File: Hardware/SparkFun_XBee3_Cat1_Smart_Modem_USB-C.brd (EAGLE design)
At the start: 35.6 x 59.7 mm, 107 parts, among them J3 USB Female Type C Connector, J4 QWIIC_RIGHT_ANGLE, U2 AP63203, U5 ESD Diode, U7 FT231XS

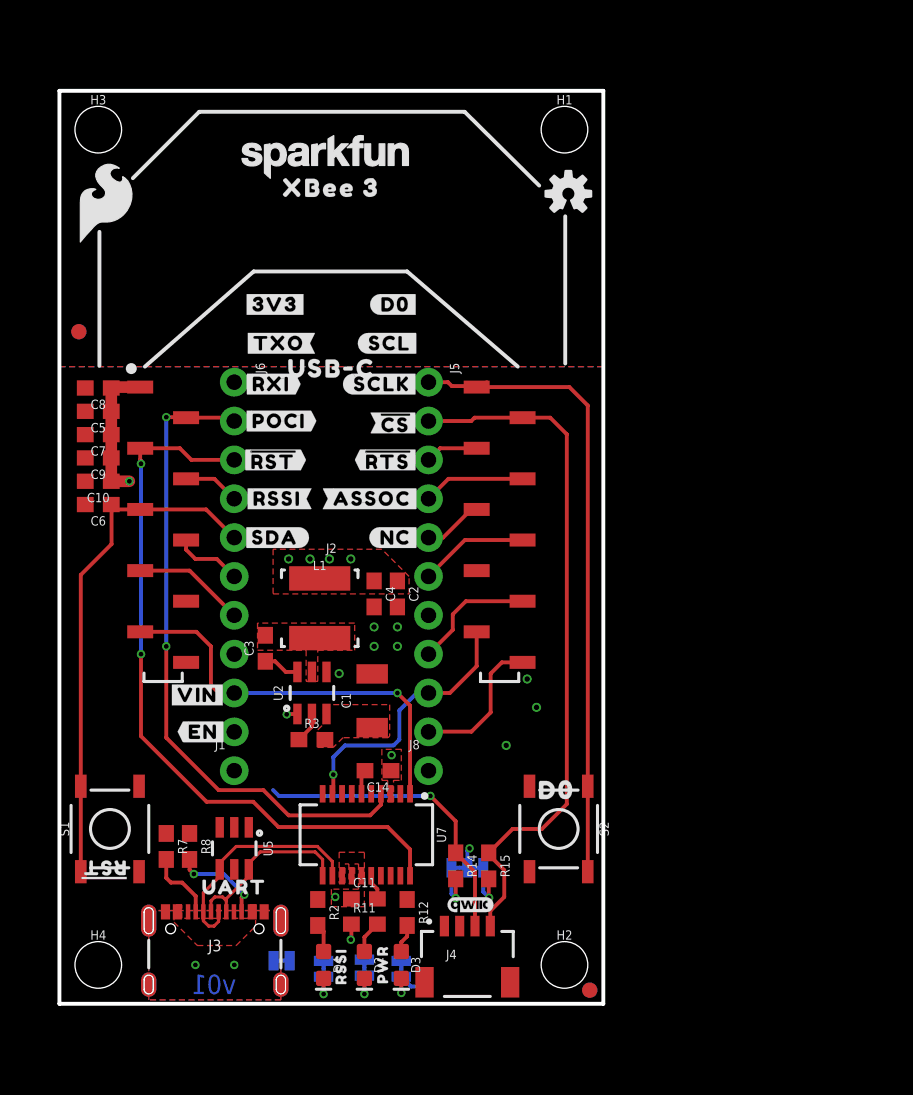
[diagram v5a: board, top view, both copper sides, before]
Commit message: Finishes routing airwires, fixes silk
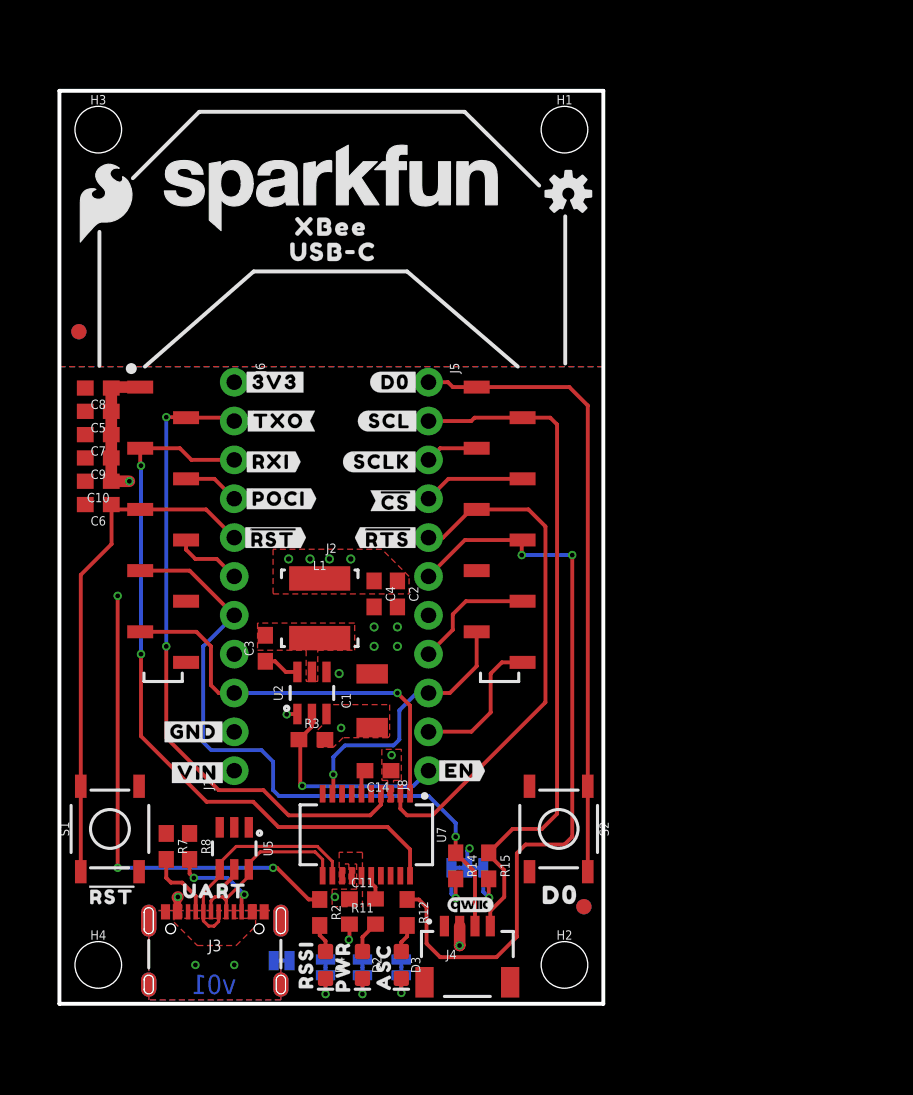
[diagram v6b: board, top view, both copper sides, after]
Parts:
- removed U$53: (no value), top:XBEE_335
- removed U$55: (no value), topmirror:#RSSI#16
- removed U$56: (no value), botmirror:#SDA#10
- removed U$57: (no value), botmirror:#ASSOC#28
- added U$29: (no value), top:ASC32
- added U$3: (no value), topmirror:#GND#0
- LOGO1: value SFE_LOGO_NAME.1_INCH -> SFE_LOGO_NAME.2_INCH; device SparkFun-Aesthetics:SFE_LOGO_NAME_.1 -> SparkFun-Aesthetics:SFE_LOGO_NAME_.2
- U$1: device topmirror:RSSI31 -> top:RSSI31
- U$10: device botmirror:#NC#3 -> top:XBEE340
- U$2: device topmirror:PWR29 -> top:PWR29
- U$23: device top:XBEE_335 -> top:XBEE340
- moved U$10 20.7 mm to (17.8, 50.8)
- moved U$48 17.0 mm to (26.2, 15.2), flipped to the top
- moved U$67 17.0 mm to (26.2, 15.2), flipped to the bottom
- moved U$4 7.67 mm to (11.0, 2.79), turned to 0 degrees
- moved U$24 7.62 mm to (17.9, 49.1)
- moved U$40 6.86 mm to (32.8, 7.11)
- moved FD3 5.47 mm to (34.3, 6.35)
- moved FD4 5.47 mm to (34.3, 6.35)
- moved U$46 5.21 mm to (9.02, 15.1)
- moved U$5 5.08 mm to (9.27, 22.9)
- moved U$14 5.08 mm to (6.99, 27.9)
- moved U$15 5.08 mm to (7.24, 25.4)
- moved U$35 5.08 mm to (29.2, 27.9)
- moved U$36 5.08 mm to (27.9, 22.9)
- moved U$38 5.08 mm to (28.4, 17.7)
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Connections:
- removed net VIN: J1.1
- net V_USB: now also J1.1
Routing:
- net D5/ASSOCIATE: track 7.64 -> 50.1 mm, vias 0 -> 2
- net D10/RSSI_PWM: track 5.50 -> 44.9 mm, vias 0 -> 3
- net D6/!RTS!: track 3.91 -> 34.1 mm
- net V_USB: track 0.00 -> 23.3 mm, vias 0 -> 3
- net D11/SDA: track 27.5 -> 43.5 mm
- net EN: track 2.02 -> 13.8 mm, vias 0 -> 1
- net 3.3V: track 22.5 -> 23.8 mm, vias 10 -> 11
- net D1/SCL: track 46.4 -> 45.2 mm
- net D0: track 42.3 -> 41.5 mm
- net GND: track 3.83 -> 3.37 mm, vias 8 -> 5
- removed copper zone on layer 1, net VIN

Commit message: Adds many GND vias
* Adds ordering instructions
* Changes VUSB net to VIN for consistency with other Xbee products
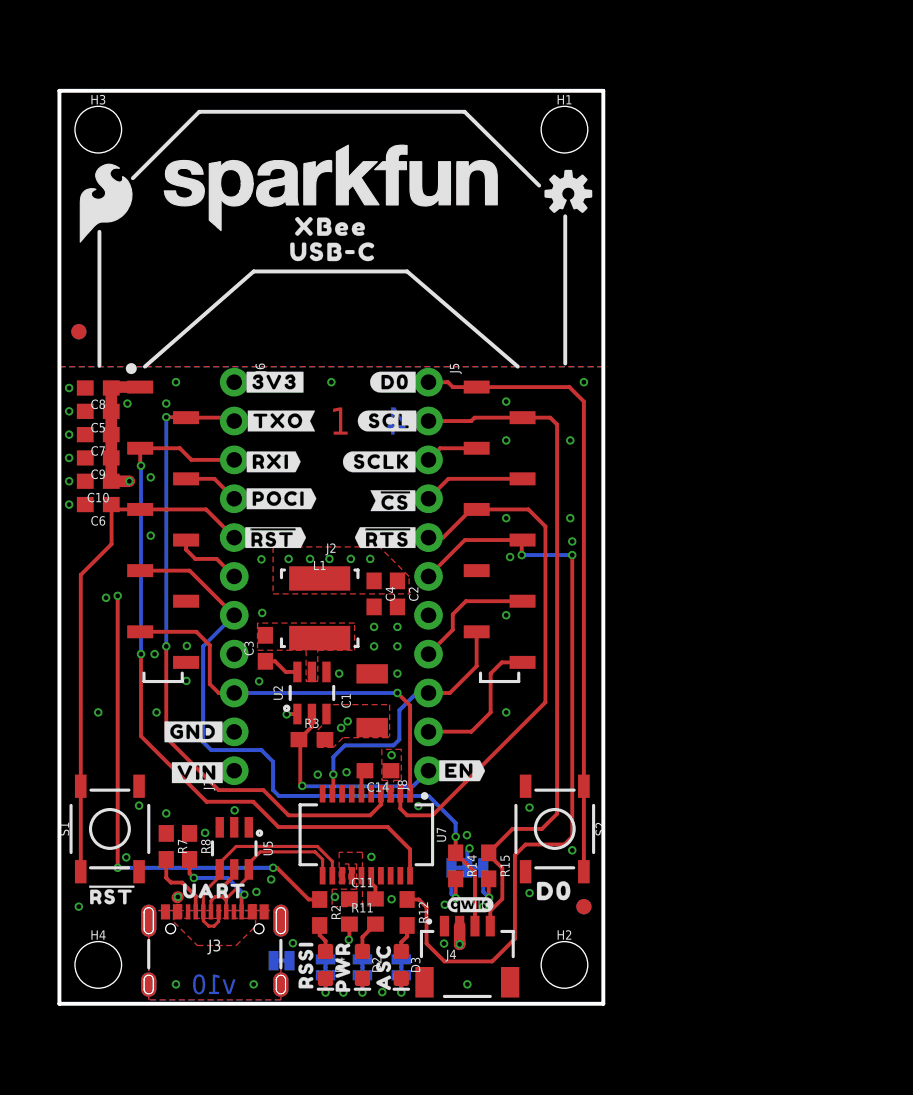
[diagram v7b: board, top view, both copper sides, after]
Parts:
- added LOGO4: SPECIAL_INSTRUCTIONS-ORDERING, SparkFun-Aesthetics:ORDERING_INSTRUCTIONS
- moved U$40 0.46 mm to (32.4, 7.37)
- moved S2 0.25 mm to (32.4, 11.4)
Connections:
- net V_USB renamed VIN
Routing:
- net VIN: track 23.3 -> 22.6 mm, vias 3 -> 4
- net 3.3V: track 23.8 -> 23.7 mm, vias 11 -> 12
- net GND: vias 5 -> 61
- added copper zone on layer 1, net V_USB
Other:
- board text added: "1"
- board text added: "1.6mm Thickness"
- board text added: "2"
- board text added: "3"
- board text added: "4"
- board text added: "Four Layer Board"
- board text added: "Lead Free HASL"
- board text added: "v10"
- board text removed: "v01"

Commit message: Replaces RED LED with the correct one
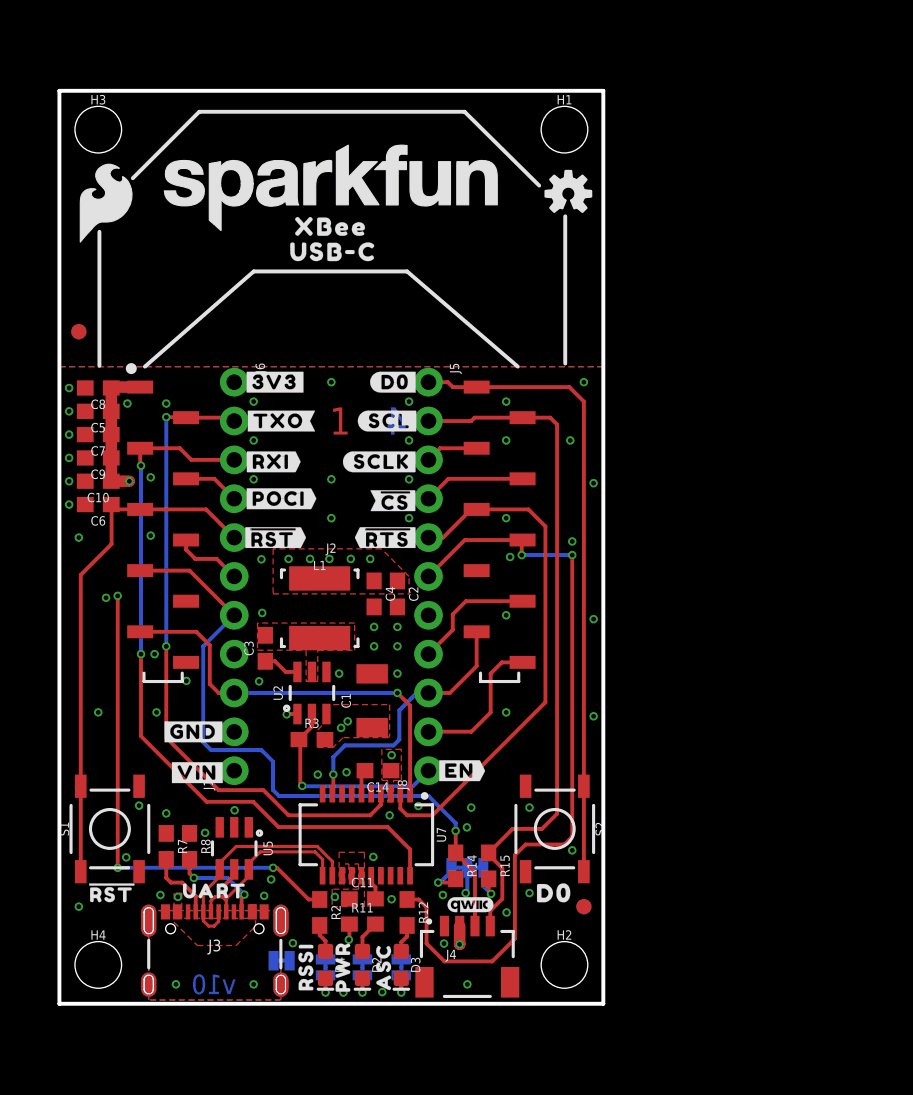
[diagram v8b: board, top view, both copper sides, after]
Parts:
- U$11: device topmirror:#D1#AD1#8 -> topmirror:#D1#AD1#SCL#8
- moved U$26 3.30 mm to (26.7, 10.5)
- moved U$11 1.78 mm to (29.7, 38.1)
- moved U$30 0.14 mm to (3.43, 7.25)
- moved U$40 0.14 mm to (32.4, 7.23)
- moved U$1 0.13 mm to (16.1, 2.41)
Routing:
- net N$11: track 3.36 -> 2.64 mm
- net GND: vias 61 -> 74
- removed copper zone on layer 1, net V_USB
